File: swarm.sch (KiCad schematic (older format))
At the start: 25 parts, among them P1 USB_OTG, P2 CONN_01X05, P3 CONN_02X20, SW1 SW_PUSH, U1 LM3671MF-3.3, U2 STM32F103RETx, U3 APA102, Y1 Crystal

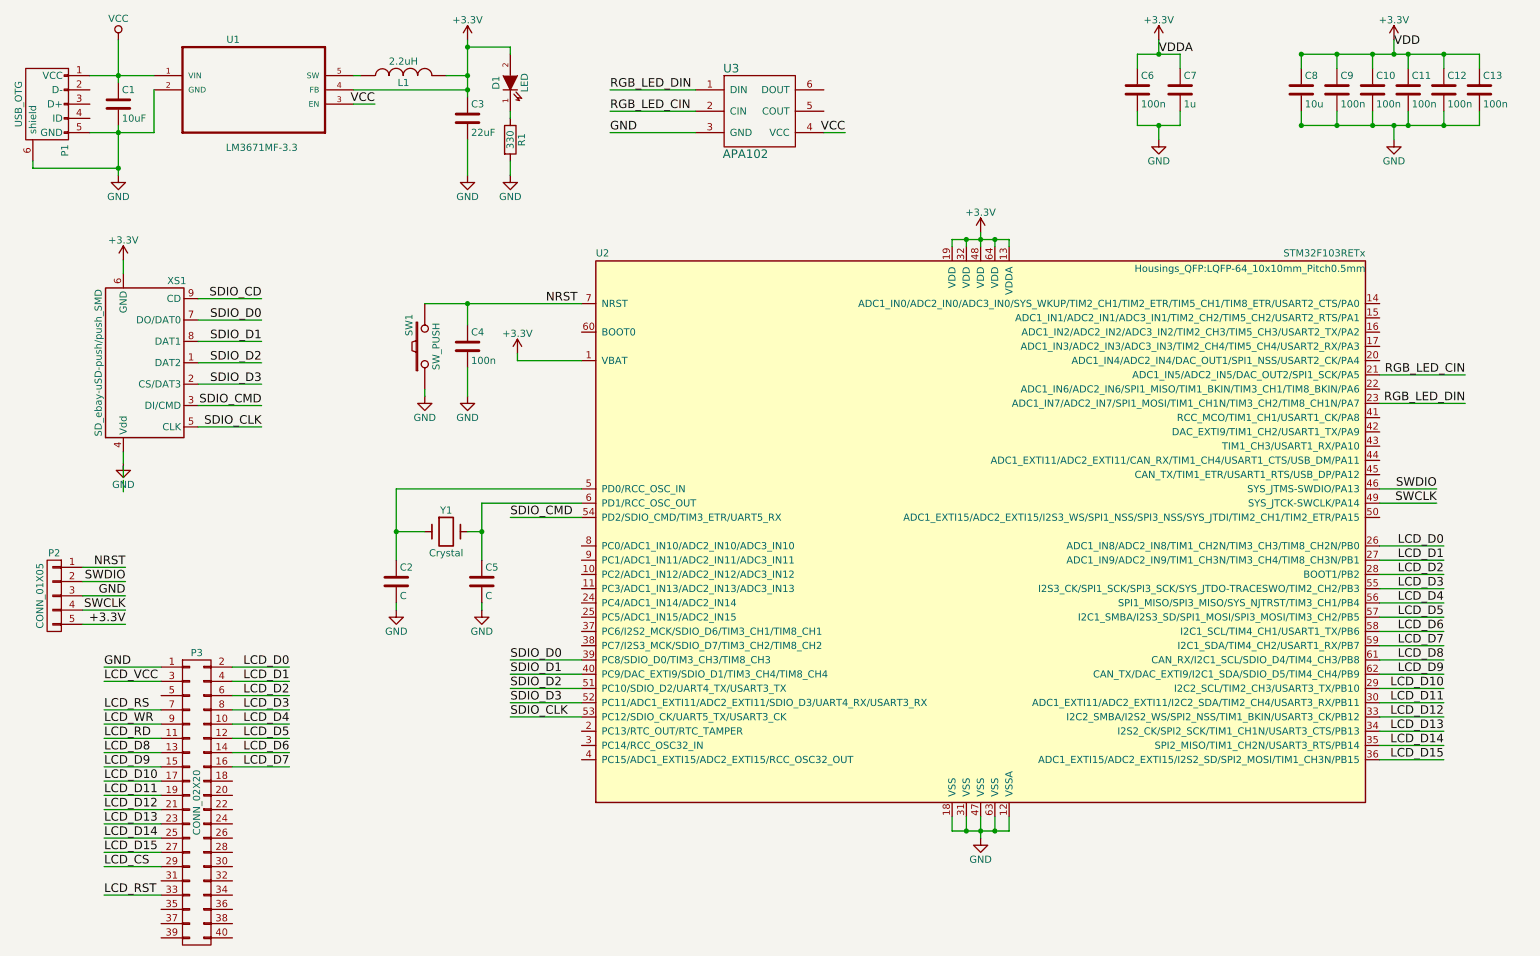
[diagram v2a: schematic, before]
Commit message: Moving towards routing Switched to 0805 components Locked connectors and MCU, routed part of LCD_DBXX signals
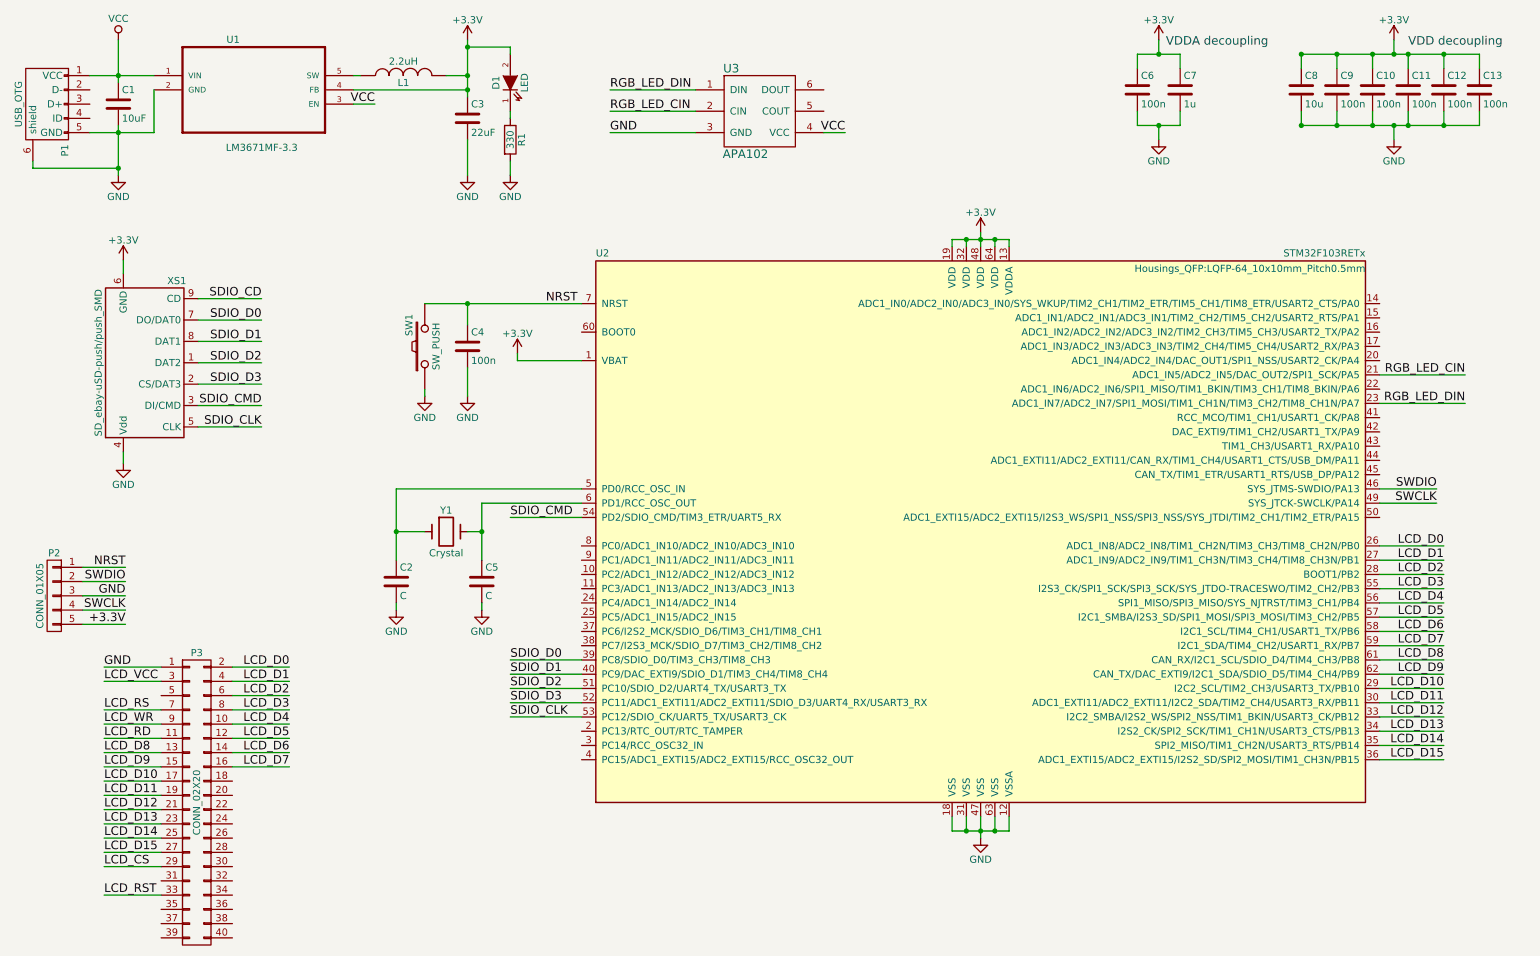
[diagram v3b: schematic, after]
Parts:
- C1, C10, C11, C12, C13, C2, C3, C4, C5, C6, C7, C8, C9: footprint Capacitors_SMD:C_1206 -> Capacitors_SMD:C_0805
- D1: footprint LEDs:LED_1206 -> LEDs:LED_0805
- R1: footprint Resistors_SMD:R_1206 -> Resistors_SMD:R_0805
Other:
- note added: "VDD decoupling"
- note added: "VDDA decoupling"
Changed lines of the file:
@@
 F 0 "C10" H 10225 1200 50  0000 L CNN
 F 1 "100n" H 10225 1000 50  0000 L CNN
-F 2 "Capacitors_SMD:C_1206" H 10238 950 50  0001 C CNN
+F 2 "Capacitors_SMD:C_0805" H 10238 950 50  0001 C CNN
 F 3 "" H 10200 1100 50  0000 C CNN
 	1    10200 1100
@@
 F 0 "C11" H 10475 1200 50  0000 L CNN
 F 1 "100n" H 10475 1000 50  0000 L CNN
-F 2 "Capacitors_SMD:C_1206" H 10488 950 50  0001 C CNN
+F 2 "Capacitors_SMD:C_0805" H 10488 950 50  0001 C CNN
 F 3 "" H 10450 1100 50  0000 C CNN
 	1    10450 1100
@@
 F 0 "C12" H 10725 1200 50  0000 L CNN
 F 1 "100n" H 10725 1000 50  0000 L CNN
-F 2 "Capacitors_SMD:C_1206" H 10738 950 50  0001 C CNN
+F 2 "Capacitors_SMD:C_0805" H 10738 950 50  0001 C CNN
 F 3 "" H 10700 1100 50  0000 C CNN
 	1    10700 1100
@@
 F 0 "C6" H 8575 1200 50  0000 L CNN
 F 1 "100n" H 8575 1000 50  0000 L CNN
-F 2 "Capacitors_SMD:C_1206" H 8588 950 50  0001 C CNN
+F 2 "Capacitors_SMD:C_0805" H 8588 950 50  0001 C CNN
 F 3 "" H 8550 1100 50  0000 C CNN
 	1    8550 1100
@@
 F 0 "C9" H 9975 1200 50  0000 L CNN
 F 1 "100n" H 9975 1000 50  0000 L CNN
-F 2 "Capacitors_SMD:C_1206" H 9988 950 50  0001 C CNN
+F 2 "Capacitors_SMD:C_0805" H 9988 950 50  0001 C CNN
 F 3 "" H 9950 1100 50  0000 C CNN
 	1    9950 1100
@@
 F 0 "C8" H 9725 1200 50  0000 L CNN
 F 1 "10u" H 9725 1000 50  0000 L CNN
-F 2 "Capacitors_SMD:C_1206" H 9738 950 50  0001 C CNN
+F 2 "Capacitors_SMD:C_0805" H 9738 950 50  0001 C CNN
 F 3 "" H 9700 1100 50  0000 C CNN
 	1    9700 1100
@@
 F 0 "C7" H 8875 1200 50  0000 L CNN
 F 1 "1u" H 8875 1000 50  0000 L CNN
-F 2 "Capacitors_SMD:C_1206" H 8888 950 50  0001 C CNN
+F 2 "Capacitors_SMD:C_0805" H 8888 950 50  0001 C CNN
 F 3 "" H 8850 1100 50  0000 C CNN
 	1    8850 1100
@@
 F 0 "C4" H 3875 3000 50  0000 L CNN
 F 1 "100n" H 3875 2800 50  0000 L CNN
-F 2 "Capacitors_SMD:C_1206" H 3888 2750 50  0001 C CNN
+F 2 "Capacitors_SMD:C_0805" H 3888 2750 50  0001 C CNN
 F 3 "" H 3850 2900 50  0000 C CNN
 	1    3850 2900
@@
 F 0 "C2" H 3375 4650 50  0000 L CNN
 F 1 "C" H 3375 4450 50  0000 L CNN
-F 2 "Capacitors_SMD:C_1206" H 3388 4400 50  0001 C CNN
+F 2 "Capacitors_SMD:C_0805" H 3388 4400 50  0001 C CNN
 F 3 "" H 3350 4550 50  0000 C CNN
 	1    3350 4550
@@
 F 0 "C5" H 3975 4650 50  0000 L CNN
 F 1 "C" H 3975 4450 50  0000 L CNN
-F 2 "Capacitors_SMD:C_1206" H 3988 4400 50  0001 C CNN
+F 2 "Capacitors_SMD:C_0805" H 3988 4400 50  0001 C CNN
 F 3 "" H 3950 4550 50  0000 C CNN
 	1    3950 4550
@@
 F 0 "C1" H 1425 1300 50  0000 L CNN
 F 1 "10uF" H 1425 1100 50  0000 L CNN
-F 2 "Capacitors_SMD:C_1206" H 1438 1050 50  0001 C CNN
+F 2 "Capacitors_SMD:C_0805" H 1438 1050 50  0001 C CNN
 F 3 "" H 1400 1200 50  0000 C CNN
 	1    1400 1200
@@
 F 0 "C3" H 3875 1400 50  0000 L CNN
 F 1 "22uF" H 3875 1200 50  0000 L CNN
-F 2 "Capacitors_SMD:C_1206" H 3888 1150 50  0001 C CNN
+F 2 "Capacitors_SMD:C_0805" H 3888 1150 50  0001 C CNN
 F 3 "" H 3850 1300 50  0000 C CNN
 	1    3850 1300
@@
 F 0 "D1" H 4150 1150 50  0000 C CNN
 F 1 "LED" H 4150 950 50  0000 C CNN
-F 2 "LEDs:LED_1206" H 4150 1050 50  0001 C CNN
+F 2 "LEDs:LED_0805" H 4150 1050 50  0001 C CNN
 F 3 "" H 4150 1050 50  0000 C CNN
 	1    4150 1050
@@
 F 0 "R1" V 4230 1450 50  0000 C CNN
 F 1 "330" V 4150 1450 50  0000 C CNN
-F 2 "Resistors_SMD:R_1206" V 4080 1450 50  0001 C CNN
+F 2 "Resistors_SMD:R_0805" V 4080 1450 50  0001 C CNN
 F 3 "" H 4150 1450 50  0000 C CNN
 	1    4150 1450
@@
 Text Label 10650 3900 2    60   ~ 0
 SWDIO
-Text Label 8700 850  0    60   ~ 0
-VDDA
-Text Label 10350 800  0    60   ~ 0
-VDD
 $Comp
 L APA102 U3
@@
 F 0 "C13" H 10975 1200 50  0000 L CNN
 F 1 "100n" H 10975 1000 50  0000 L CNN
-F 2 "Capacitors_SMD:C_1206" H 10988 950 50  0001 C CNN
+F 2 "Capacitors_SMD:C_0805" H 10988 950 50  0001 C CNN
 F 3 "" H 10950 1100 50  0000 C CNN
 	1    10950 1100
@@
 Wire Wire Line
 	1435 3720 1435 3640
-Wire Wire Line
-	1435 3820 1435 3740
-Wire Wire Line
-	1435 3920 1435 3840
 Wire Wire Line
 	1700 5150 1300 5150
@@
 Wire Wire Line
 	7650 2150 7650 2200
+Text Notes 8750 800  0    60   ~ 0
+VDDA decoupling
+Text Notes 10450 800  0    60   ~ 0
+VDD decoupling
 $EndSCHEMATC

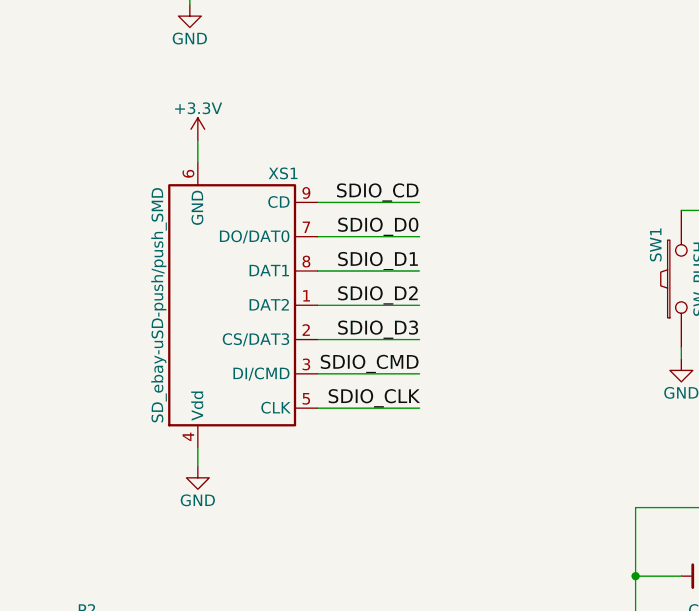
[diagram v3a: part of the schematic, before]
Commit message: All LCD DBXX signals routed
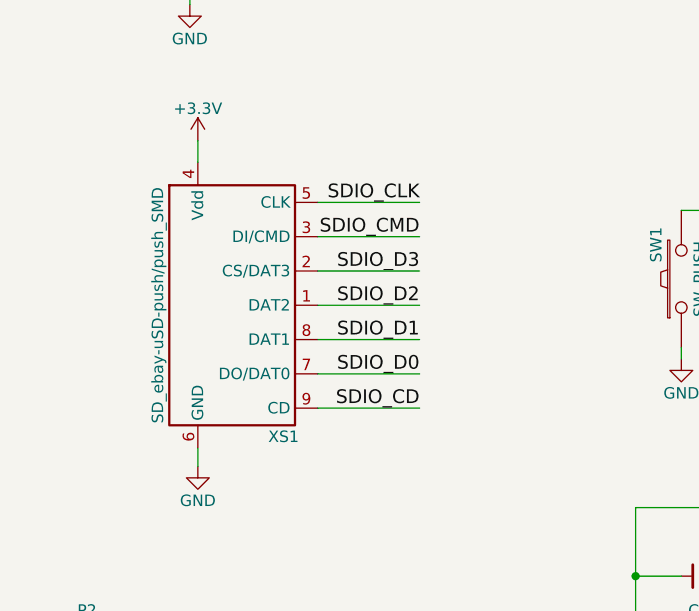
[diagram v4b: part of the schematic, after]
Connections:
- net +3V3: now also XS1.4 (Vdd); no longer XS1.6 (GND)
- net GND: now also XS1.6 (GND); no longer XS1.4 (Vdd)
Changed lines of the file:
@@
 F 5 "ebay" H 1585 3015 10  0001 C CNN "Manf"
 	1    1585 3015
-	1    0    0    1
+	1    0    0    -1
 $EndComp
 Text Label 4150 5100 0    60   ~ 0
@@
 Text Label 4150 4100 0    60   ~ 0
 SDIO_CMD
-Text Label 2405 3465 2    60   ~ 0
+Text Label 2405 2565 2    60   ~ 0
 SDIO_CLK
-Text Label 2405 2715 2    60   ~ 0
+Text Label 2405 3315 2    60   ~ 0
 SDIO_D0
-Text Label 2405 2865 2    60   ~ 0
+Text Label 2405 3165 2    60   ~ 0
 SDIO_D1
 Text Label 2405 3015 2    60   ~ 0
 SDIO_D2
-Text Label 2405 3165 2    60   ~ 0
+Text Label 2405 2865 2    60   ~ 0
 SDIO_D3
-Text Label 2405 3315 2    60   ~ 0
+Text Label 2405 2715 2    60   ~ 0
 SDIO_CMD
-Text Label 2405 2565 2    60   ~ 0
+Text Label 2405 3465 2    60   ~ 0
 SDIO_CD
 $Comp
@@
 	4650 4100 4150 4100
 Wire Wire Line
+	1960 3465 2405 3465
+Wire Wire Line
+	1960 3315 2405 3315
+Wire Wire Line
+	1960 3165 2405 3165
+Wire Wire Line
+	1960 3015 2405 3015
+Wire Wire Line
+	1960 2865 2405 2865
+Wire Wire Line
+	1960 2715 2405 2715
+Wire Wire Line
 	1960 2565 2405 2565
 Wire Wire Line
-	1960 2715 2405 2715
-Wire Wire Line
-	1960 2865 2405 2865
-Wire Wire Line
-	1960 3015 2405 3015
-Wire Wire Line
-	1960 3165 2405 3165
-Wire Wire Line
-	1960 3315 2405 3315
-Wire Wire Line
-	1960 3465 2405 3465
-Wire Wire Line
 	1435 2295 1435 2390
